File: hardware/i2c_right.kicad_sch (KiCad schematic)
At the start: 18 parts, among them J1 INPUT USB, U1 TPS259261, U2 AP2125N-3.3TRG1

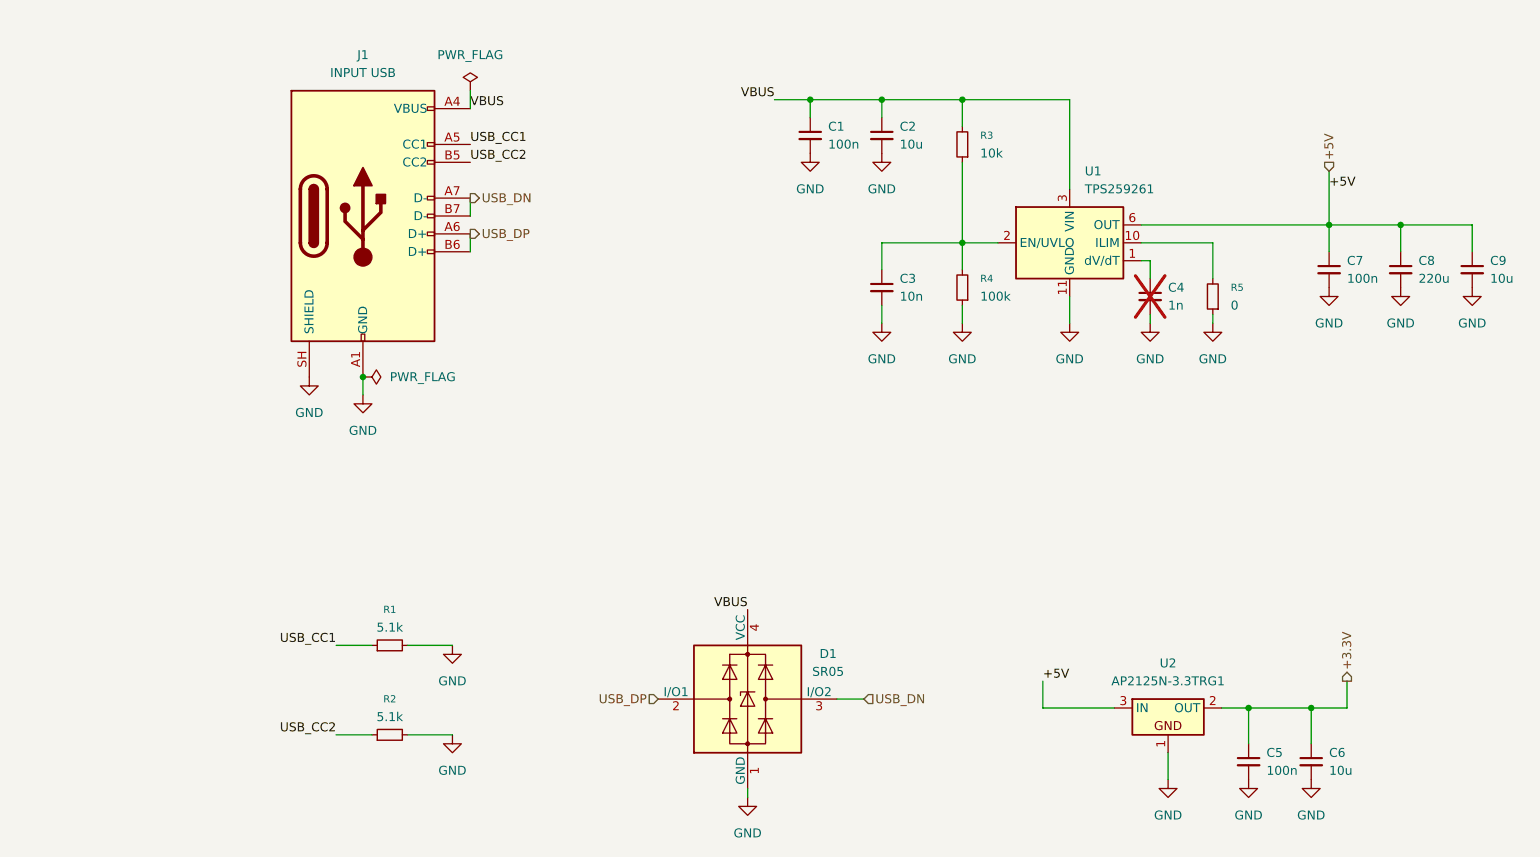
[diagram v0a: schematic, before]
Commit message: separate left/right part design, schematic
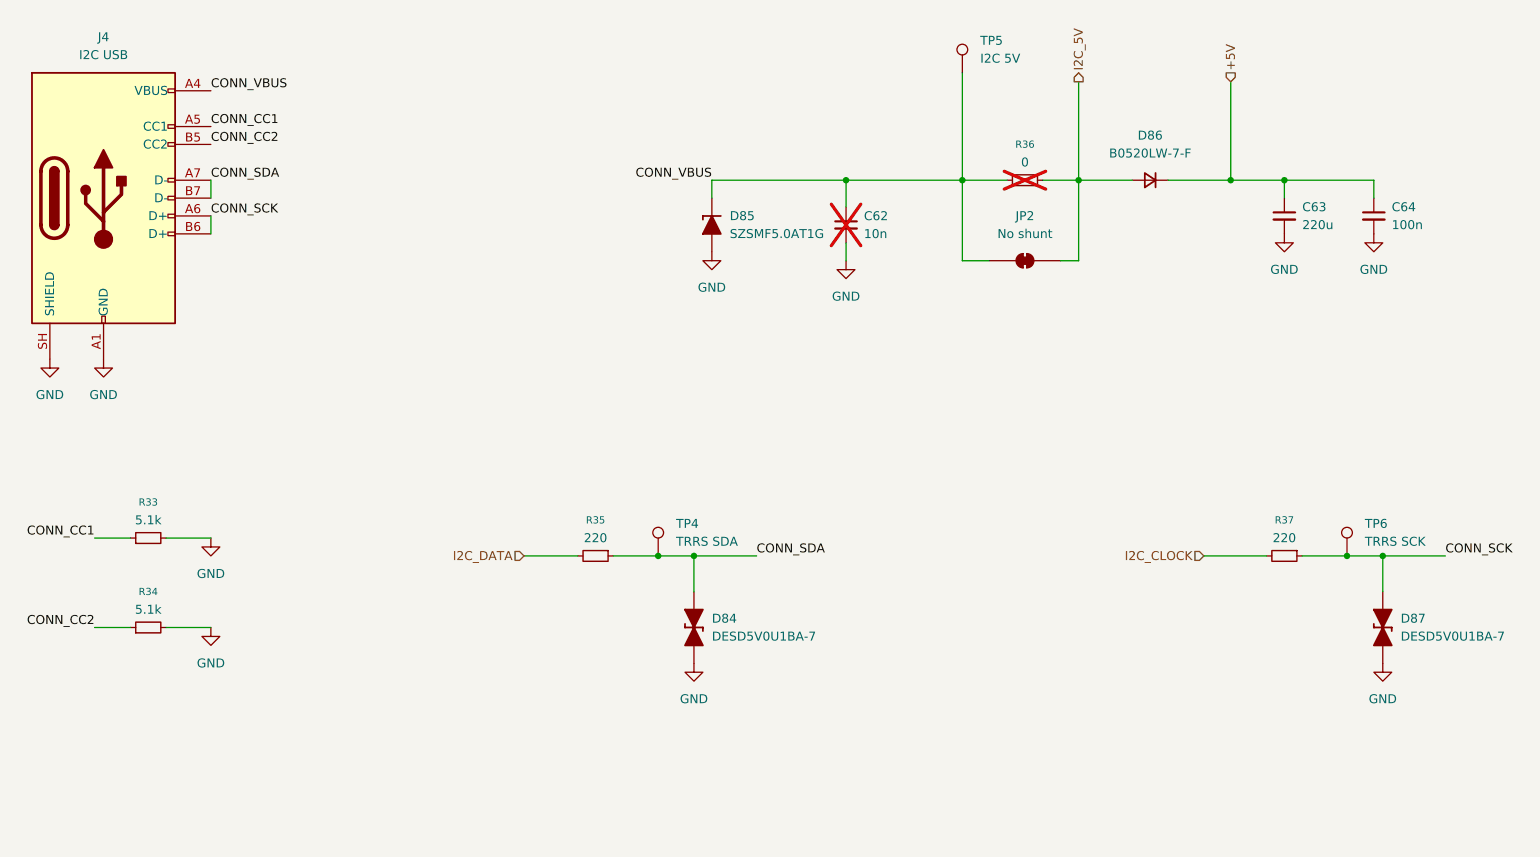
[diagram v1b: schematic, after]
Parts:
- removed C1, C5, C7: 100n, PCM_Capacitor_SMD_AKL:C_0603_1608Metric_Pad1.05x0.95mm_HandSolder, symbol Device:C_Small
- removed C2: 10u, PCM_Capacitor_SMD_AKL:C_0603_1608Metric_Pad1.05x0.95mm_HandSolder, symbol Device:C_Small
- removed C3: 10n, PCM_Capacitor_SMD_AKL:C_0603_1608Metric_Pad1.05x0.95mm_HandSolder, symbol Device:C_Small
- removed C4: 1n, PCM_Capacitor_SMD_AKL:C_0603_1608Metric_Pad1.05x0.95mm_HandSolder, symbol Device:C_Small
- removed C6, C9: 10u, PCM_Capacitor_SMD_AKL:C_0805_2012Metric_Pad1.15x1.40mm_HandSolder, symbol Device:C_Small
- removed C8: 220u, PCM_Capacitor_SMD_AKL:C_1210_3225Metric_Pad1.33x2.70mm_HandSolder, symbol Device:C_Small
- removed D1: SR05, Package_TO_SOT_SMD:SOT-143, symbol Power_Protection:PRTR5V0U2X
- removed J1: INPUT USB, Connector_USB:USB_C_Receptacle_GCT_USB4105-xx-A_16P_TopMnt_Horizontal, symbol Connector:USB_C_Receptacle_USB2.0_14P
- removed R1, R2: 5.1k, PCM_Resistor_SMD_AKL:R_0603_1608Metric_Pad0.98x0.95mm_HandSolder, symbol Device:R_Small
- removed R3: 10k, PCM_Resistor_SMD_AKL:R_0603_1608Metric, symbol Device:R_Small
- removed R4: 100k, PCM_Resistor_SMD_AKL:R_0603_1608Metric, symbol Device:R_Small
- removed R5: 0, PCM_Resistor_SMD_AKL:R_0603_1608Metric_Pad0.98x0.95mm_HandSolder, symbol Device:R_Small
- removed U1: TPS259261, Package_SON:VSON-10-1EP_3x3mm_P0.5mm_EP1.65x2.4mm_ThermalVias, symbol Power_Management:TPS2592xx
- removed U2: AP2125N-3.3TRG1, PCM_Package_TO_SOT_SMD_AKL:SOT-23, symbol PCM_Voltage_Regulator_AKL:AP2125N-3.3TRG1
- added C62: 10n, PCM_Capacitor_SMD_AKL:C_0603_1608Metric_Pad1.05x0.95mm_HandSolder, symbol Device:C_Small
- added C63: 220u, PCM_Capacitor_SMD_AKL:C_1210_3225Metric_Pad1.33x2.70mm_HandSolder, symbol Device:C_Small
- added C64: 100n, PCM_Capacitor_SMD_AKL:C_0603_1608Metric, symbol Device:C_Small
- added D84, D87: DESD5V0U1BA-7, PCM_Diode_SMD_AKL:D_SOD-323_HandSoldering, symbol PCM_Diode_TVS_AKL:D_TVS_Bidirectional_Generic
- added D85: SZSMF5.0AT1G, PCM_Diode_SMD_Handsoldering_AKL:D_SOD-123_TVS, symbol PCM_Diode_TVS_AKL:D_TVS_Unidirectional_Generic
- added D86: B0520LW-7-F, PCM_Diode_SMD_AKL:D_SOD-123, symbol Device:D_Small
- added J4: I2C USB, Connector_USB:USB_C_Receptacle_GCT_USB4105-xx-A_16P_TopMnt_Horizontal, symbol Connector:USB_C_Receptacle_USB2.0_14P
- added JP2: No shunt, Jumper:SolderJumper-2_P1.3mm_Bridged_RoundedPad1.0x1.5mm, symbol Jumper:SolderJumper_2_Bridged
- added R33, R34: 5.1k, PCM_Resistor_SMD_AKL:R_0603_1608Metric_Pad0.98x0.95mm_HandSolder, symbol Device:R_Small
- added R35, R37: 220, PCM_Resistor_SMD_AKL:R_0603_1608Metric_Pad0.98x0.95mm_HandSolder, symbol Device:R_Small
- added R36: 0, PCM_Resistor_SMD_AKL:R_1206_3216Metric_Pad1.30x1.75mm_HandSolder, symbol Device:R_Small
- added TP4: TRRS SDA, TestPoint:TestPoint_Pad_D2.0mm, symbol Connector:TestPoint
- added TP5: I2C 5V, TestPoint:TestPoint_Pad_D2.0mm, symbol Connector:TestPoint
- added TP6: TRRS SCK, TestPoint:TestPoint_Pad_D2.0mm, symbol Connector:TestPoint
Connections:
- net +5V: now also C63.1, C64.1, D86.1 (K)
- net GND: now also C62.2, C63.2, C64.2, D84.1 (K), D85.2 (A), D87.1 (K), J4.A1 (GND), J4.A12 (GND), J4.B1 (GND), J4.B12 (GND), J4.SH (SHIELD), R33.2, R34.2
- new net CONN_CC1: J4.A5 (CC1), R33.1
- new net CONN_CC2: J4.B5 (CC2), R34.1
- new net CONN_SCK: D87.2 (A), J4.A6 (D+), J4.B6 (D+), R37.1, TP6.1
- new net CONN_SDA: D84.2 (A), J4.A7 (D-), J4.B7 (D-), R35.1, TP4.1
- new net CONN_VBUS: C62.1, D85.1 (K), J4.A4 (VBUS), J4.A9 (VBUS), J4.B4 (VBUS), J4.B9 (VBUS), JP2.1 (A), R36.2, TP5.1
- new net I2C_5V: D86.2 (A), JP2.2 (B), R36.1
- new net I2C_CLOCK: R37.2
- new net I2C_DATA: R35.2
